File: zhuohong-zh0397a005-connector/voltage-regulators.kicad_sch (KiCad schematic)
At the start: 10 parts, among them U1 RS3236-2.5FY5, U3 AP3127B

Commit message: Add LCSC numbers to C's and R's
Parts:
- C1, C2, C3, C6: LCSC (none) -> C5189821
- R3: lcsc C166772 -> C3013206
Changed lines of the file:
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@@
 			)
 		)
-		(property "lcsc" "C166772"
+		(property "lcsc" "C3013206"
 			(at 232.41 58.42 0)
 			(effects
@@
 			)
 		)
+		(property "LCSC" "C5189821"
+			(at 186.69 59.69 0)
+			(effects
+				(font
+					(size 1.27 1.27)
+				)
+				(hide yes)
+			)
+		)
+		(property "Field6" ""
+			(at 186.69 59.69 0)
+			(effects
+				(font
+					(size 1.27 1.27)
+				)
+				(hide yes)
+			)
+		)
 		(pin "1"
 		)
@@
 			)
 		)
+		(property "LCSC" "C5189821"
+			(at 90.17 46.99 0)
+			(effects
+				(font
+					(size 1.27 1.27)
+				)
+				(hide yes)
+			)
+		)
 		(pin "2"
 		)
@@
 			)
 		)
+		(property "LCSC" "C5189821"
+			(at 102.87 41.91 0)
+			(effects
+				(font
+					(size 1.27 1.27)
+				)
+				(hide yes)
+			)
+		)
 		(pin "2"
 		)
@@
 			(at 35.56 41.91 0)
 			(effects
+				(font
+					(size 1.27 1.27)
+				)
+				(hide yes)
+			)
+		)
+		(property "LCSC" "C5189821"
+			(at 35.56 41.91 0)
+			(effects
+				(font
+					(size 1.27 1.27)
+				)
+				(hide yes)
+			)
+		)
+		(property "Field6" ""
+			(at 35.56 41.91 0)
+			(effects

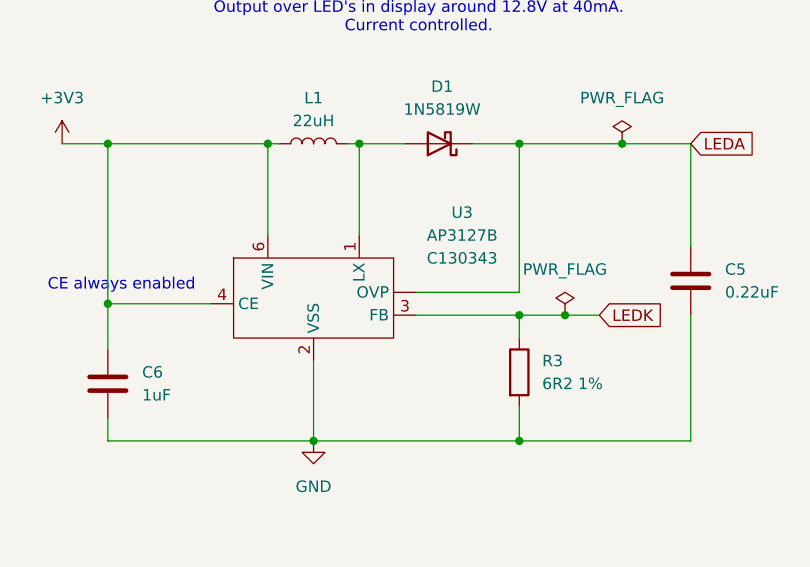
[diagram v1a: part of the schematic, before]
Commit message: Fix names, footprints, and silkscreen of the pcb's
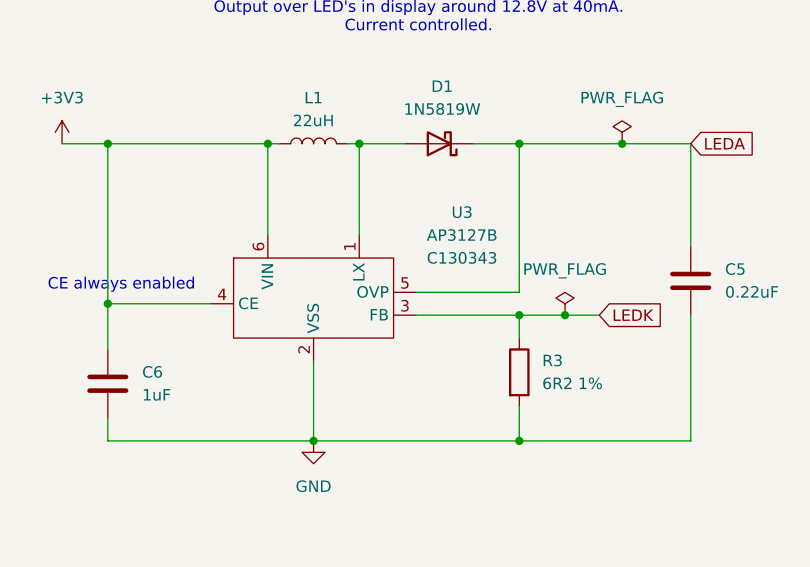
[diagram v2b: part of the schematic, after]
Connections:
- net LEDA: now also U3.5 (OVP); no longer U3. (OVP)
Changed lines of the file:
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@@
 		(pin "1"
 		)
-		(pin ""
+		(pin "5"
 		)
 		(pin "2"

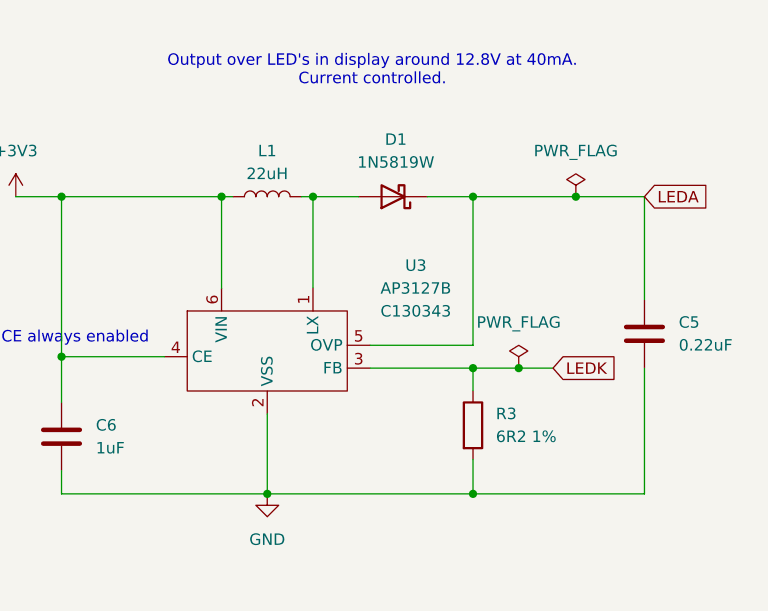
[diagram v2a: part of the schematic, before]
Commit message: Fixed lmt040wv004c board for production @ JLCPCB
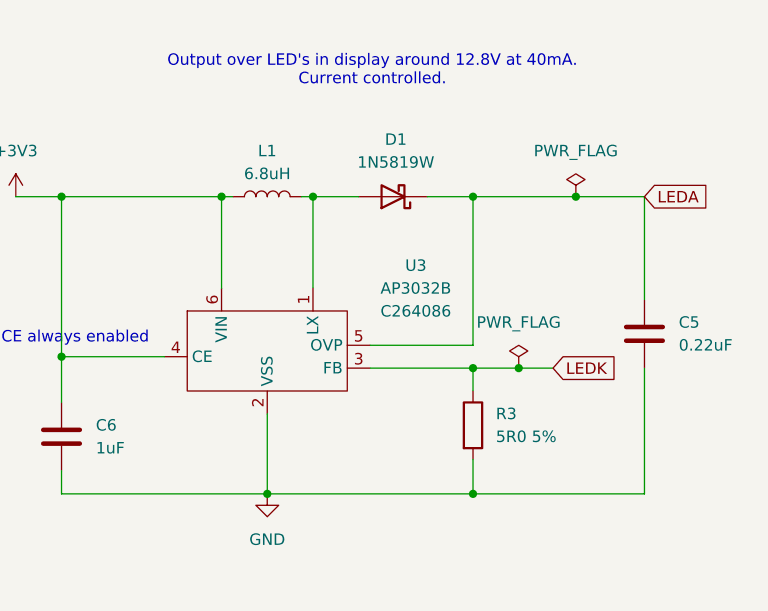
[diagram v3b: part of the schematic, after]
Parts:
- C1, C2, C3, C6: LCSC C5189821 -> C386149
- L1: value 22uH -> 6.8uH; footprint Inductor_SMD:L_Changjiang_FNR252010S -> Inductor_SMD:L_1210_3225Metric; LCSC C486445 -> C394999
- R3: value 6R2 1% -> 5R0 5%; LCSC (none) -> C2907176; lcsc C3013206 -> (none)
- U1: LCSC (none) -> C379345; Lcsc C379345 -> (none)
- U3: value AP3127B -> AP3032B; LCSC C130343 -> C264086
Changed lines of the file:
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@@
 			)
 		)
-		(property "Value" "AP3127B"
+		(property "Value" "AP3032B"
 			(at 226.06 43.2114 0)
 			(effects
@@
 			)
 		)
-		(property "Datasheet" "https://file.remont-aud.net/baza/dc_dc/data/AP3127B.pdf"
+		(property "Datasheet" "https://datasheet.lcsc.com/lcsc/1808151350_Diodes-Incorporated-AP3032KTR-G1_C264086.pdf"
 			(at 204.47 50.8 0)
 			(effects
@@
 			)
 		)
-		(property "LCSC" "C130343"
+		(property "LCSC" "C264086"
 			(at 226.06 45.7514 0)
 			(effects
@@
 			)
 		)
-		(property "Value" "6R2 1%"
+		(property "Value" "5R0 5%"
 			(at 234.95 59.6899 0)
 			(effects
@@
 			)
 		)
-		(property "lcsc" "C3013206"
+		(property "LCSC" "C2907176"
 			(at 232.41 58.42 0)
 			(effects
@@
 			)
 		)
-		(property "LCSC" "C5189821"
+		(property "LCSC" "C386149 "
 			(at 186.69 59.69 0)
 			(effects
@@
 			)
 		)
-		(property "LCSC" "C5189821"
+		(property "LCSC" "C386149 "
 			(at 90.17 46.99 0)
 			(effects
@@
 			)
 		)
-		(property "Lcsc" "C379345"
+		(property "LCSC" "C379345"
 			(at 64.77 45.72 0)
 			(effects
@@
 			)
 		)
-		(property "LCSC" "C5189821"
+		(property "LCSC" "C386149 "
 			(at 102.87 41.91 0)
 			(effects
@@
 			)
 		)
-		(property "Value" "22uH"
+		(property "Value" "6.8uH"
 			(at 209.55 30.48 90)
 			(effects
@@
 			)
 		)
-		(property "Footprint" "Inductor_SMD:L_Changjiang_FNR252010S"
+		(property "Footprint" "Inductor_SMD:L_1210_3225Metric"
 			(at 209.55 33.02 0)
 			(effects
@@
 			)
 		)
-		(property "Datasheet" "https://www.lcsc.com/datasheet/lcsc_datasheet_2002271926_microgate-MPIT252012-220M-LF_C486445.pdf"
+		(property "Datasheet" "https://datasheet.lcsc.com/lcsc/2302231030_FH--Guangdong-Fenghua-Advanced-Tech-CMI322513X6R8KT_C394999.pdf"
 			(at 209.55 33.02 0)
 			(effects
@@
 			)
 		)
-		(property "LCSC" "C486445"
+		(property "LCSC" "C394999 "
 			(at 209.55 33.02 90)
 			(effects
@@
 			)
 		)
-		(property "LCSC" "C5189821"
+		(property "LCSC" "C386149 "
 			(at 35.56 41.91 0)
 			(effects
